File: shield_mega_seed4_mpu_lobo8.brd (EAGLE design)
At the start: 99.3 x 72.4 mm, 32 parts, among them U1 GY-521MPU6050

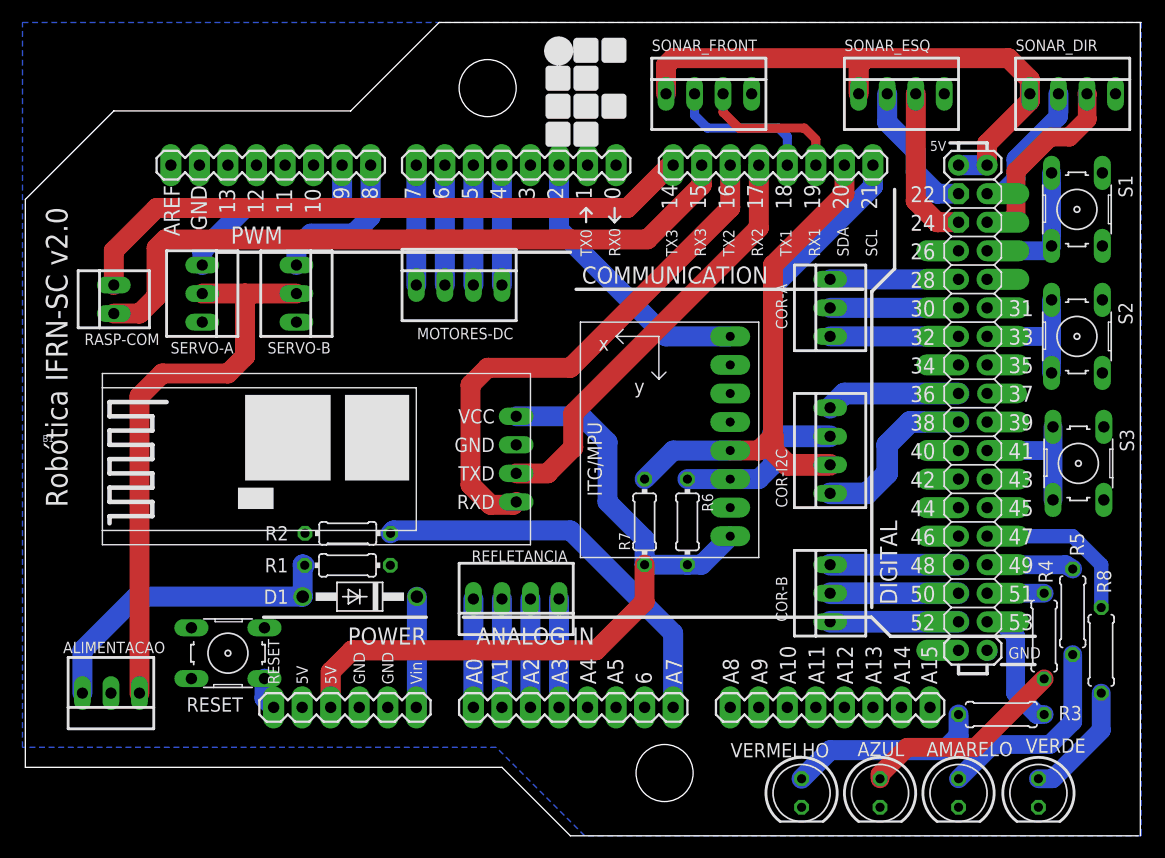
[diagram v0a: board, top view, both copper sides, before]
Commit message: Adicionado o conector para o novo modelo da placa.
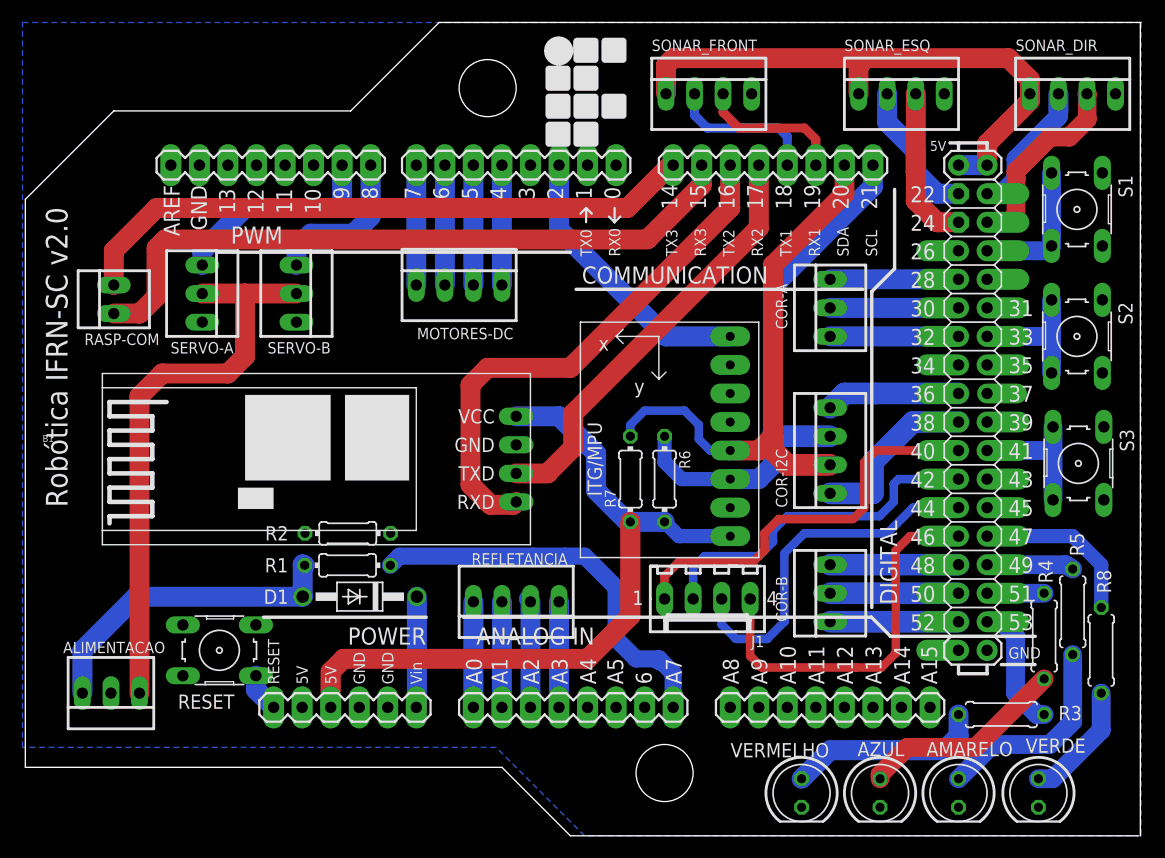
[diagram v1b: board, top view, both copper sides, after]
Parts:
- added J1: CONN_0427-2041, Robotica-IFRN-SC-conectores:6410-04
- moved R6 4.32 mm to (56.4, 40.6)
- moved R7 4.02 mm to (53.3, 40.6)
- moved RESET 0.80 mm to (16.8, 25.4)
- moved REFLETANCIA 0.25 mm to (43.2, 29.7)
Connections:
- new net N$44: B1.40, J1.1
- new net N$45: B1.42, J1.2
- new net N$46: B1.44, J1.3
- new net N$47: B1.46, J1.4
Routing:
- net N$44: track 0.00 -> 36.1 mm
- net N$47: track 0.00 -> 34.2 mm
- net N$46: track 0.00 -> 32.3 mm
- net N$45: track 0.00 -> 31.2 mm
- net SCL: track 43.7 -> 48.6 mm
- net SDA: track 46.6 -> 50.6 mm
- net +5V/1: track 67.0 -> 65.7 mm
- net N$31: track 2.90 -> 3.47 mm
